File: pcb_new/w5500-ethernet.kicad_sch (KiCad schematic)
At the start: 59 parts, among them J8 ARJM11B1-009-AB-EW2, U4 W5500

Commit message: initial test of new board
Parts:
- C125, C49: Mouser Part Number 81-GRM15C61E475ME15J -> (none)
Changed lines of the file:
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@@
 			)
 		)
-		(property "Mouser Part Number" "81-GRM15C61E475ME15J"
+		(property "Mouser Part Number" ""
 			(at 38.1 773.66 0)
 			(effects
@@
 			)
 		)
-		(property "Mouser Part Number" "81-GRM15C61E475ME15J"
+		(property "Mouser Part Number" ""
 			(at 160.02 873.99 0)
 			(effects

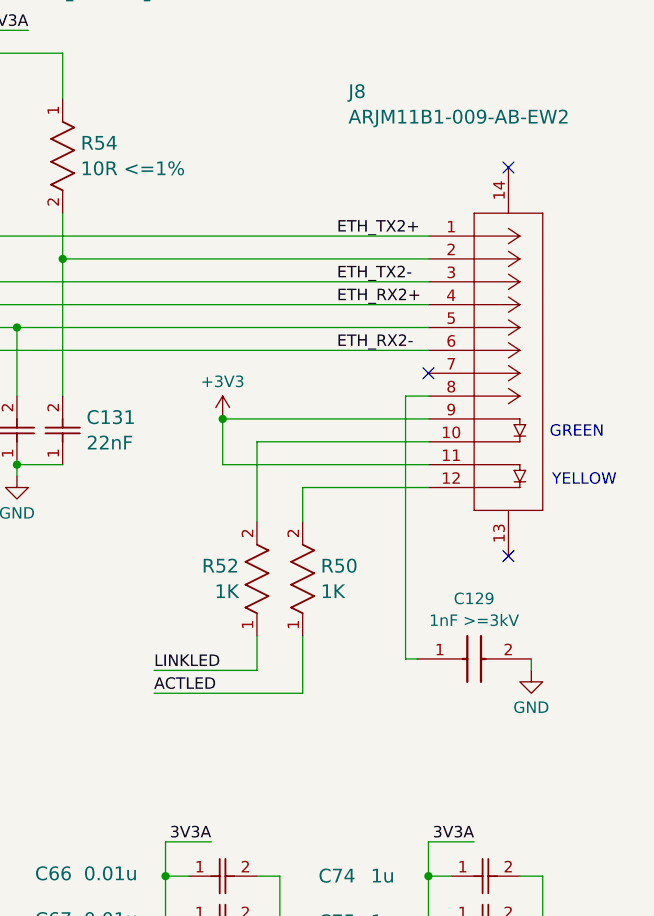
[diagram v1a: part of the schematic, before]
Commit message: ground ethernet chassis mounts (ref #58)
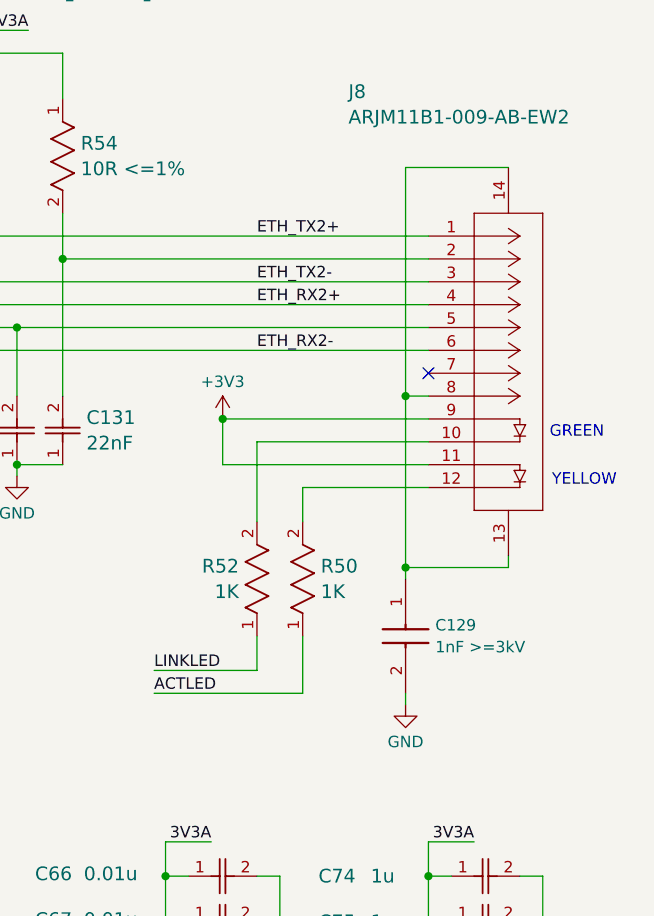
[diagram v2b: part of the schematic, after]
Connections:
- net at C129.1, J8.8: now also J8.13, J8.14
- no-connect marks 14 -> 12
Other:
- moved on the sheet: C129
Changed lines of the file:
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@@
 	)
 	(junction
+		(at 259.08 88.9)
+		(diameter 0)
+		(color 0 0 0 0)
+	)
+	(junction
 		(at 102.87 77.47)
 		(diameter 0)
@@
 	)
 	(junction
+		(at 259.08 69.85)
+		(diameter 0)
+		(color 0 0 0 0)
+	)
+	(junction
 		(at 245.11 138.43)
 		(diameter 0)
@@
 	)
 	(no_connect
-		(at 270.51 87.63)
-	)
-	(no_connect
 		(at 99.06 52.07)
 	)
@@
 	)
 	(no_connect
-		(at 270.51 44.45)
-	)
-	(no_connect
 		(at 99.06 44.45)
 	)
@@
 	(wire
 		(pts
-			(xy 273.05 99.06) (xy 273.05 100.33)
+			(xy 259.08 102.87) (xy 259.08 104.14)
 		)
 		(stroke
@@
 	(wire
 		(pts
-			(xy 247.65 96.52) (xy 247.65 102.87)
-		)
-		(stroke
-			(width 0)
-			(type default)
-		)
-	)
-	(wire
-		(pts
 			(xy 261.62 74.93) (xy 242.57 74.93)
 		)
@@
 	(wire
 		(pts
+			(xy 270.51 44.45) (xy 259.08 44.45)
+		)
+		(stroke
+			(width 0)
+			(type default)
+		)
+	)
+	(wire
+		(pts
 			(xy 194.31 78.74) (xy 189.23 78.74)
 		)
@@
 	(wire
 		(pts
-			(xy 259.08 99.06) (xy 260.35 99.06)
-		)
-		(stroke
-			(width 0)
-			(type default)
-		)
-	)
-	(wire
-		(pts
 			(xy 173.99 57.15) (xy 261.62 57.15)
 		)
@@
 	(wire
 		(pts
+			(xy 270.51 87.63) (xy 270.51 88.9)
+		)
+		(stroke
+			(width 0)
+			(type default)
+		)
+	)
+	(wire
+		(pts
 			(xy 186.69 92.71) (xy 196.85 92.71)
 		)
@@
 	(wire
 		(pts
+			(xy 259.08 44.45) (xy 259.08 69.85)
+		)
+		(stroke
+			(width 0)
+			(type default)
+		)
+	)
+	(wire
+		(pts
 			(xy 261.62 119.38) (xy 261.62 123.19)
 		)
@@
 	(wire
 		(pts
-			(xy 259.08 69.85) (xy 259.08 99.06)
+			(xy 259.08 69.85) (xy 259.08 88.9)
 		)
 		(stroke
@@
 	(wire
 		(pts
+			(xy 270.51 88.9) (xy 259.08 88.9)
+		)
+		(stroke
+			(width 0)
+			(type default)
+		)
+	)
+	(wire
+		(pts
 			(xy 69.85 139.7) (xy 67.31 139.7)
 		)
@@
 	(wire
 		(pts
+			(xy 259.08 88.9) (xy 259.08 90.17)
+		)
+		(stroke
+			(width 0)
+			(type default)
+		)
+	)
+	(wire
+		(pts
 			(xy 173.99 57.15) (xy 173.99 48.26)
 		)
@@
 	(wire
 		(pts
+			(xy 247.65 96.52) (xy 247.65 102.87)
+		)
+		(stroke
+			(width 0)
+			(type default)
+		)
+	)
+	(wire
+		(pts
 			(xy 106.68 53.34) (xy 106.68 80.01)
 		)
@@
 	)
 	(label "ETH_TX2-"
-		(at 251.46 57.15 0)
+		(at 242.57 57.15 0)
 		(fields_autoplaced yes)
 		(effects
@@
 	)
 	(label "ETH_RX2-"
-		(at 251.46 64.77 0)
+		(at 242.57 64.77 0)
 		(fields_autoplaced yes)
 		(effects
@@
 	)
 	(label "ETH_TX2+"
-		(at 251.46 52.07 0)
+		(at 242.57 52.07 0)
 		(fields_autoplaced yes)
 		(effects
@@
 	)
 	(label "ETH_RX2+"
-		(at 251.46 59.69 0)
+		(at 242.57 59.69 0)
 		(fields_autoplaced yes)
 		(effects
@@
 	(symbol
 		(lib_id "OroLink:885342210004")
-		(at 260.35 99.06 0)
+		(at 259.08 90.17 270)
 		(unit 1)
 		(exclude_from_sim no)
@@
 		(fields_autoplaced yes)
 		(property "Reference" "C129"
-			(at 266.7 92.3755 0)
+			(at 262.382 95.3078 90)
 			(effects
 				(font
 					(size 1.27 1.27)
 				)
+				(justify left)
 			)
 		)
 		(property "Value" "1nF >=3kV"
-			(at 266.7 94.7998 0)
+			(at 262.382 97.7321 90)
 			(effects
 				(font
 					(size 1.27 1.27)
 				)
+				(justify left)
 			)
 		)
 		(property "Footprint" "OroLink:CAPC4620X220N"
-			(at 269.24 195.25 0)
+			(at 162.89 99.06 0)
 			(effects
 				(font
@@
 		)
 		(property "Datasheet" "https://katalog.we-online.com/pbs/datasheet/885342210004.pdf"
-			(at 269.24 295.25 0)
+			(at 62.89 99.06 0)
 			(effects
 				(font
@@
 		)
 		(property "Description" "Multilayer Ceramic Chip Capacitor WCAP-CSMH Series 1808 1000pF X7R1808102KC00DFCT10000"
-			(at 260.35 99.06 0)
+			(at 259.08 90.17 0)
 			(effects
 				(font
@@
 		)
 		(property "Height" "2.2"
-			(at 269.24 495.25 0)
+			(at -137.11 99.06 0)
 			(effects
 				(font
@@
 		)
 		(property "Manufacturer_Name" "Wurth Elektronik"
-			(at 269.24 595.25 0)
+			(at -237.11 99.06 0)
 			(effects
 				(font
@@
 		)
 		(property "Manufacturer_Part_Number" "885342210004"
-			(at 269.24 695.25 0)
+			(at -337.11 99.06 0)
 			(effects
 				(font
@@
 		)
 		(property "Mouser Part Number" "710-885342210004"
-			(at 269.24 795.25 0)
+			(at -437.11 99.06 0)
 			(effects
 				(font
@@
 		)
 		(property "Mouser Price/Stock" "https://www.mouser.co.uk/ProductDetail/Wurth-Elektronik/885342210004?qs=MLItCLRbWsya%2F3qdX09FHQ%3D%3D"
-			(at 269.24 895.25 0)
+			(at -537.11 99.06 0)
 			(effects
 				(font
@@
 		)
 		(property "Arrow Part Number" ""
-			(at 269.24 995.25 0)
+			(at -637.11 99.06 0)
 			(effects
 				(font
@@
 		)
 		(property "Arrow Price/Stock" ""
-			(at 269.24 1095.25 0)
+			(at -737.11 99.06 0)
 			(effects
 				(font
@@
 	(symbol
 		(lib_id "power:GND")
-		(at 273.05 100.33 0)
+		(at 259.08 104.14 0)
 		(unit 1)
 		(exclude_from_sim no)
@@
 		(dnp no)
 		(property "Reference" "#PWR0164"
-			(at 273.05 106.68 0)
+			(at 259.08 110.49 0)
 			(effects
 				(font
@@
 		)
 		(property "Value" "GND"
-			(at 273.05 104.4631 0)
+			(at 259.08 108.2731 0)
 			(effects
 				(font
@@
 		)
 		(property "Footprint" ""
-			(at 273.05 100.33 0)
+			(at 259.08 104.14 0)
 			(effects
 				(font
@@
 		)
 		(property "Datasheet" ""
-			(at 273.05 100.33 0)
+			(at 259.08 104.14 0)
 			(effects
 				(font
@@
 		)
 		(property "Description" "Power symbol creates a global label with name \"GND\" , ground"
-			(at 273.05 100.33 0)
+			(at 259.08 104.14 0)
 			(effects
 				(font

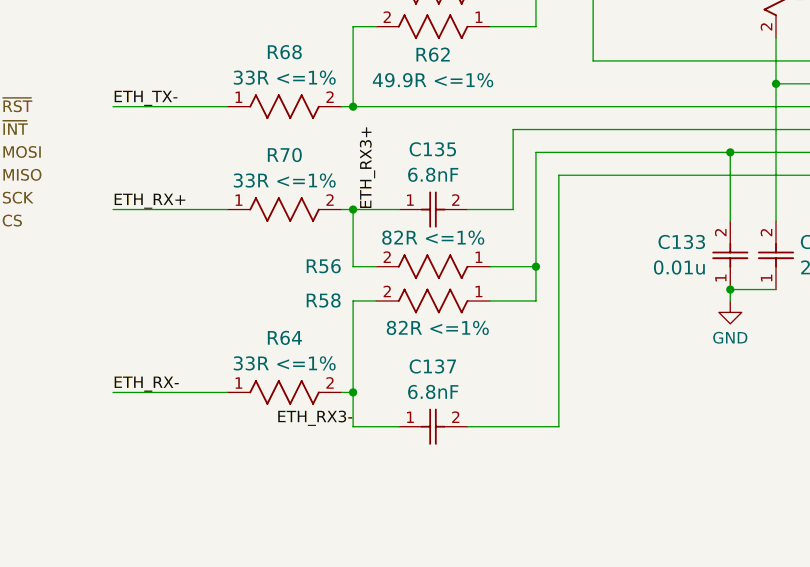
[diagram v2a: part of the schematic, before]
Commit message: replace 82R resistors on ethernet circuits with 49R9 (ref #60)
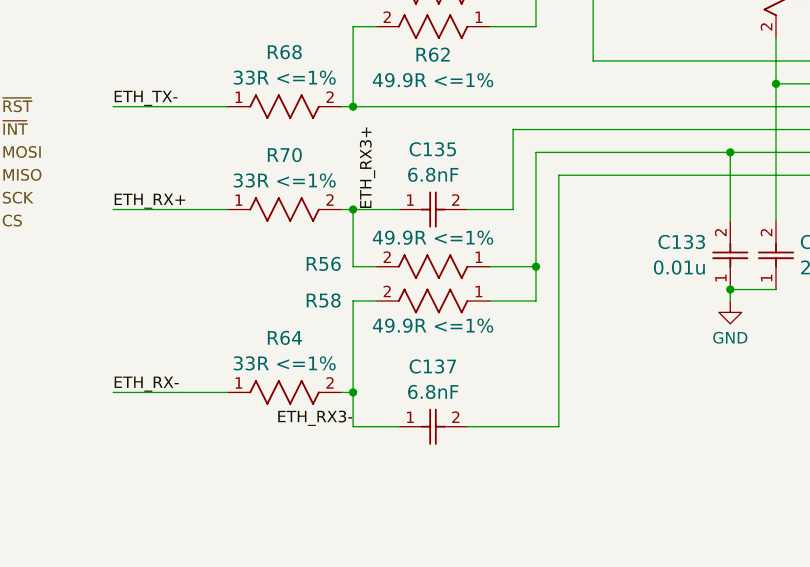
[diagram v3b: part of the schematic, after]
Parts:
- removed R56, R58: 82R <=1%, OroLink:RC0402N_PAN, symbol OroLink:ERA-2AEB820X
- added R56, R58: 49.9R <=1%, OroLink:RC0402N_YAG, symbol OroLink:RT0402FRE0749R9L
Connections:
- net ETH_RX3+: now also R56.2
- net ETH_RX3-: now also R58.2
- net at C133.2, J8.5: now also R56.1, R58.1

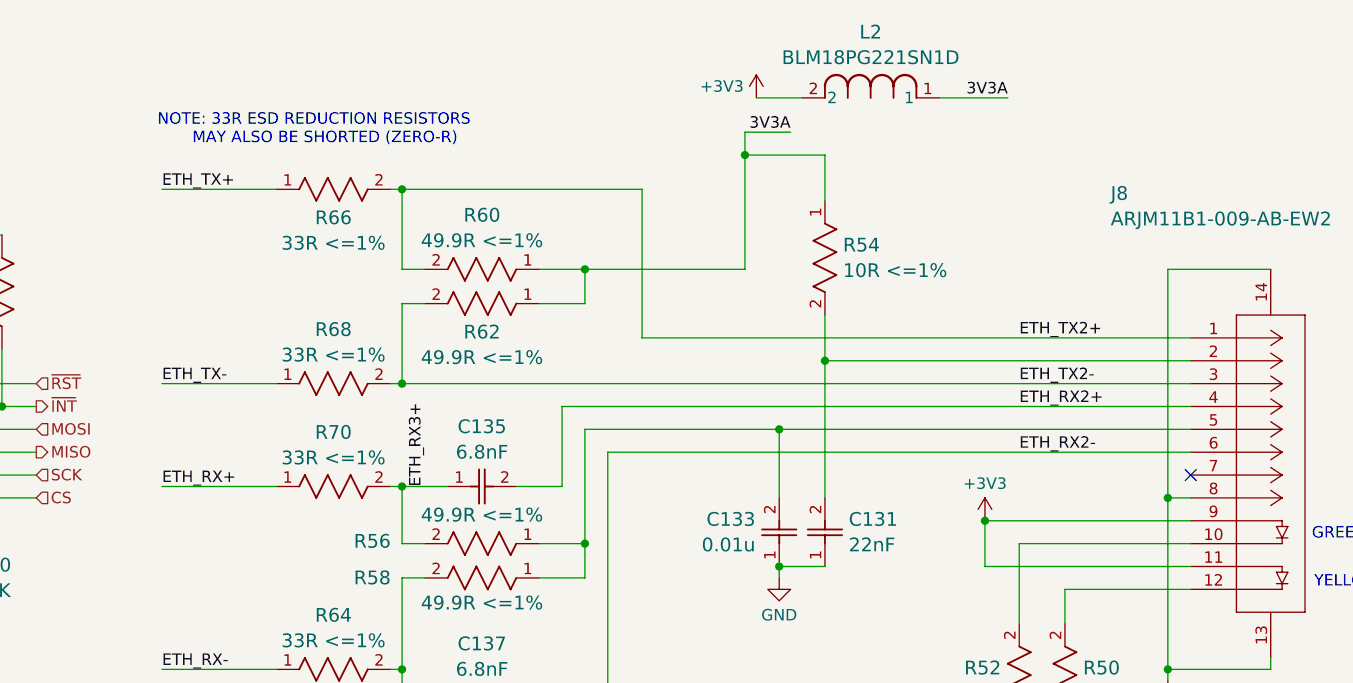
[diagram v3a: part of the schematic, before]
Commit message: correct magjack wiring (ref #61)
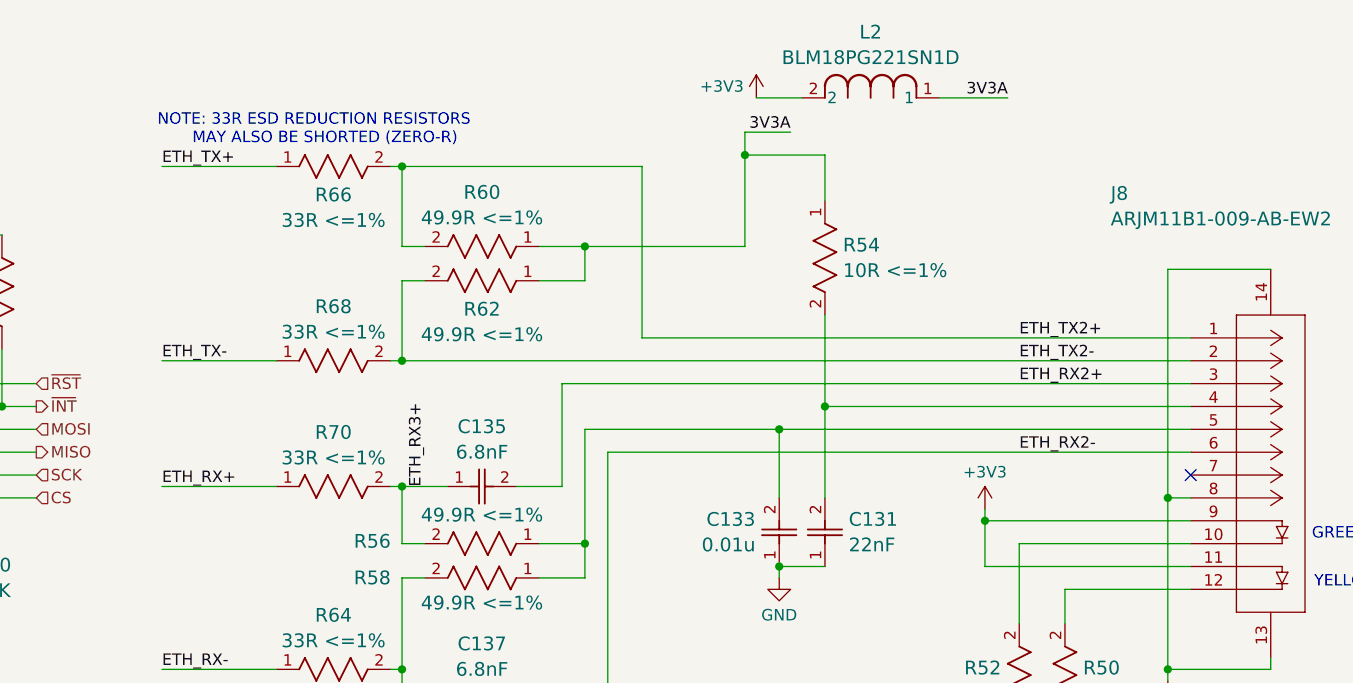
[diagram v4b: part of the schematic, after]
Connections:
- net ETH_RX2+: now also J8.3; no longer J8.4
- net ETH_TX2-: now also J8.2; no longer J8.3
- net at C131.2, R54.2: now also J8.4; no longer J8.2
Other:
- moved on the sheet: R60, R62, R66, R68

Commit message: pull up external ethernet ~{RST} line (ref #74)
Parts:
- removed R40: 10K, OroLink:STA_RMCF0402_STP, symbol OroLink:RMCF0402FT10K0
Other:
- note added: "NOTE: PULL-UP/-DOWN ON ~{RST} IS EXTERNAL TO PAGE"

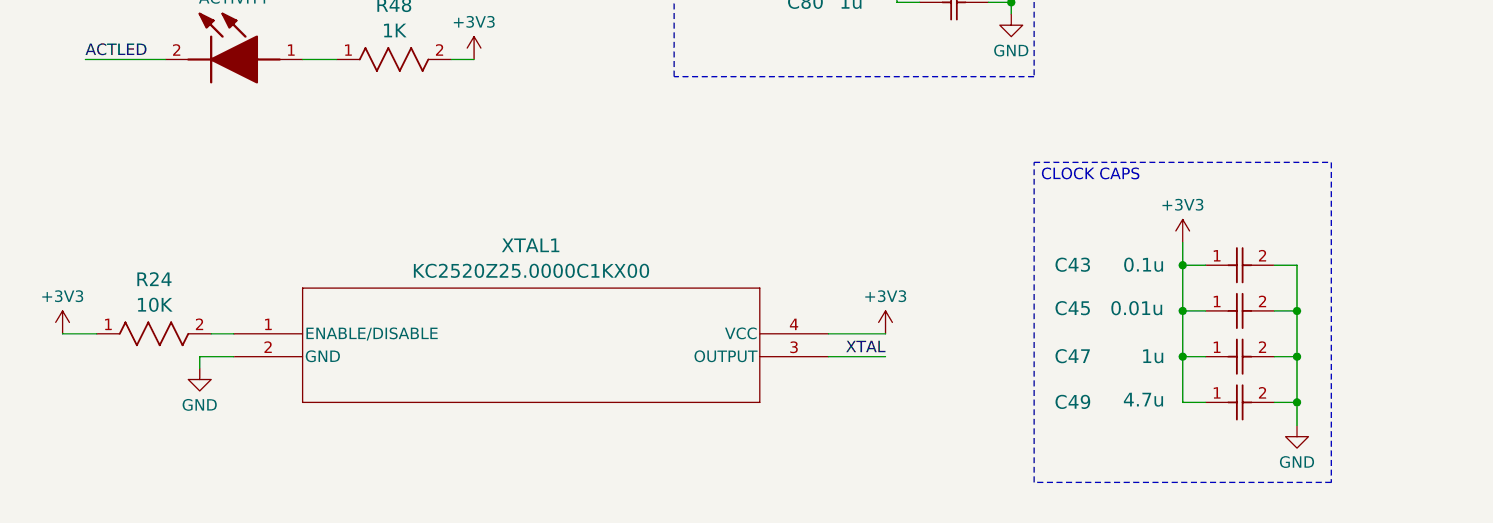
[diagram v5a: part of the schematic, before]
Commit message: replace ethernet clocks with more robust unit (ref #72)
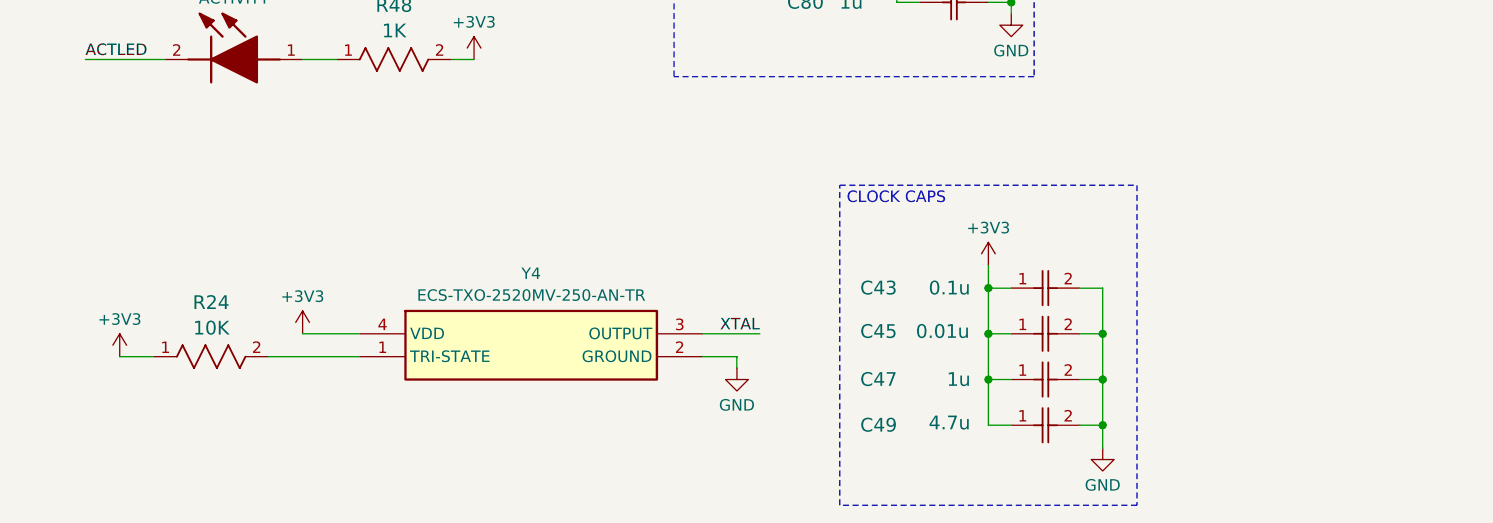
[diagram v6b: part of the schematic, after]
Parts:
- removed XTAL1: KC2520Z25.0000C1KX00, OroLink:KC2520Z25_KAV, symbol OroLink:KC2520Z25.0000C1KX00
- added Y4: ECS-TXO-2520MV-250-AN-TR, OroLink:ECSTXO2520MV250ANTR, symbol OroLink:ECS-TXO-2520MV-250-AN-TR
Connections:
- net +3V3: now also Y4.4 (VDD)
- net GND: now also Y4.2 (GROUND)
- net XTAL: now also Y4.3 (OUTPUT)
- net at R24.2: now also Y4.1 (TRI-STATE)
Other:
- moved on the sheet: C43, C45, C47, C49, R24
